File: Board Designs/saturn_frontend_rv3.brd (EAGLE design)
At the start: 40 parts

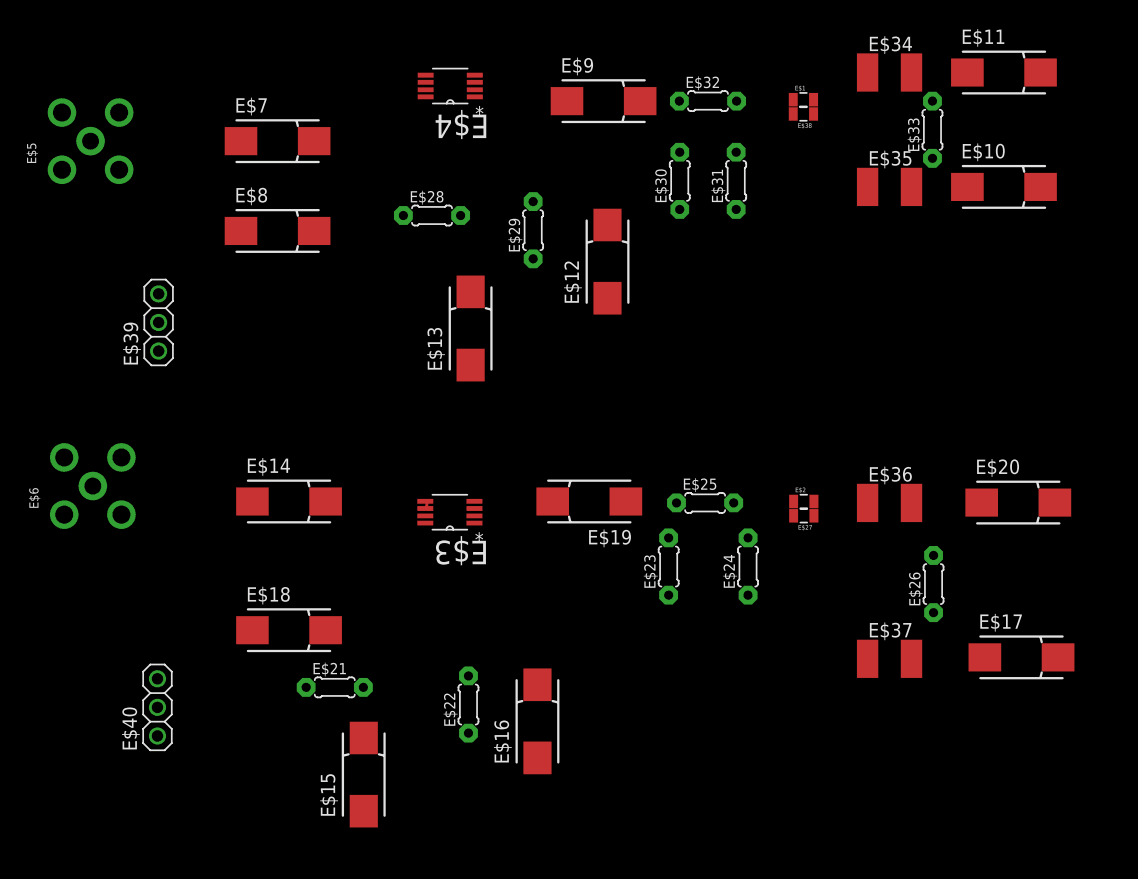
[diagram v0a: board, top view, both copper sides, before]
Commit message: Moved board designs to a seperate directory to keep SPICE/ clean
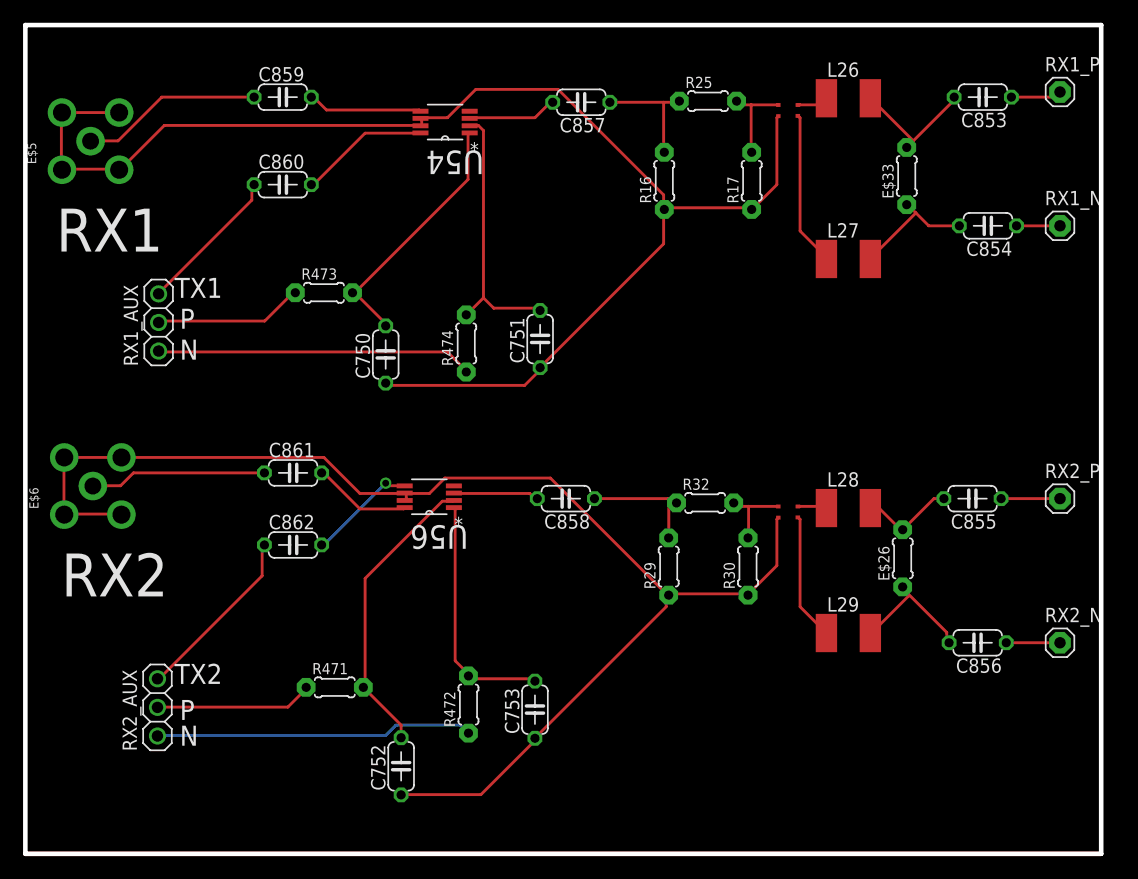
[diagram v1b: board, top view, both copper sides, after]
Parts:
- removed E$10, E$11, E$12, E$13, E$14, E$15, E$16, E$17, E$18, E$19, E$20, E$7, E$8, E$9: 100 pF, adafruit:085CS_1AR
- removed E$27, E$38: (no value), 0805:0805
- removed E$28, E$29: 100 Ohm, adafruit:0204/5
- removed E$3, E$4: (no value), SOP65P490X110-8N:SOP65P490X110-8N
- removed E$30, E$31: 221 Ohm, adafruit:0204/5
- removed E$34, E$35, E$36, E$37: 1.0 nH, eagle-ltspice:L1812
- added C750, C751, C752, C753, C853, C854, C855, C856, C857, C858, C859, C860, C861: 100 pF, adafruit:C050-024X044
- added C862: (no value), adafruit:C050-024X044
- added L26, L27, L28, L29: 1.0 nH, eagle-ltspice:L1812
- added R16, R17: 221 Ohm, adafruit:0204/5
- added R473, R474: 100 Ohm, adafruit:0204/5
- added RX1_N, RX1_P, RX2_N, RX2_P: (no value), adafruit:1X01
- added U54, U56: (no value), SOP65P490X110-8N:SOP65P490X110-8N
- E$1, E$2: device 0805:0805 -> cody_custom_library:BALUN_LOGICALS
- moved E$33 4.71 mm to (87.9, 72.1)
- moved E$26 3.57 mm to (87.5, 38.1)
- moved E$2 2.86 mm to (76.4, 41.6)
- moved E$1 2.85 mm to (76.4, 77.3)
- renumbered E$21 to R471, E$22 to R472, E$23 to R29, E$24 to R30, E$25 to R32, E$32 to R25, E$39 to RX1_AUX, E$40 to RX2_AUX
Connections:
- removed net S$17: E$2.1, R30.2, R32.2
- removed net S$21: E$12.-, E$13.-, E$30.1, E$31.1, E$38.2, E$4.6, E$4.7, E$5.GND3
- removed net S$22: E$28.2, E$4.1
- removed net S$26: E$30.2, E$9.+, R25.1
- new net S$1: E$2.1, R30.2, R32.2
- new net S$10: C857.1, R16.2, R25.1
- new net S$19: C854.2, E$33.1, L27.2
- new net S$35: C861.1, E$6.ANTENNA
- new net S$46: C752.1, C753.1, E$2.2, E$6.GND1, E$6.GND2, E$6.GND3, E$6.GND4, R29.1, R30.1, U56.6, U56.7
- new net S$47: C856.1, RX2_N.1
- new net S$49: R472.1, RX2_AUX.1
- net S$12: now also E$1.1, R17.2, R25.2; no longer E$11.-, E$33.2, E$34.2
- net S$14: now also E$1.4, L26.1; no longer E$14.+, E$15.-, E$16.-, E$27.2, E$3.5, E$3.6, E$3.7, E$6.GND3, R29.1, R30.1
- net S$16: now also E$1.3, L27.1; no longer E$4.5, E$7.+
- net S$18: now also C853.2, E$33.2, L26.2; no longer E$4.8, E$8.+
- net S$2: now also E$2.4, L28.1; no longer E$13.+
- net S$23: now also C853.1, RX1_P.1; no longer E$29.2, E$4.2
- net S$24: now also C854.1, RX1_N.1; no longer E$2.2, E$36.1
- net S$25: now also R473.1, RX1_AUX.2; no longer E$29.1, RX1_AUX.1
- net S$27: now also C750.2, R473.2, U54.1; no longer E$1.1, E$31.2, R25.2
- net S$28: now also C751.2, R474.2, U54.2; no longer E$1.2, E$34.1
- net S$29: now also R474.1, RX1_AUX.1; no longer E$35.1, E$38.1
- net S$3: now also C858.1, R29.2, R32.1; no longer E$12.+
- net S$32: now also R471.1, RX2_AUX.2; no longer E$18.-, RX2_AUX.3
- net S$33: now also C752.2, R471.2, U56.2; no longer R471.1, RX2_AUX.2
- net S$34: now also C753.2, R472.2, U56.1; no longer R472.1, RX2_AUX.1
- net S$36: now also C862.1, RX2_AUX.3; no longer E$14.-, E$6.ANTENNA
- net S$37: now also C860.1, RX1_AUX.3; no longer E$4.3, E$9.-
- net S$38: now also C859.1, E$5.ANTENNA; no longer E$18.+, E$3.8
- net S$39: now also C859.2, U54.5; no longer E$19.+, E$3.3
- net S$40: now also C860.2, U54.8; no longer E$15.+, E$3.1, R471.2
- net S$41: now also C862.2, U56.5; no longer E$16.+, E$3.2, R472.2
- net S$42: now also C861.2, U56.8; no longer E$19.-, R29.2, R32.1
- net S$43: now also C858.2, U56.3; no longer E$27.1, E$37.1
- net S$44: now also C857.2, U54.3; no longer E$20.-, E$26.2, E$36.2
- net S$45: now also C750.1, C751.1, E$1.2, E$5.GND1, E$5.GND2, E$5.GND3, E$5.GND4, R16.1, R17.1, U54.6, U54.7; no longer E$17.-, E$26.1, E$37.2
- net S$5: now also C855.2, E$26.2, L28.2; no longer E$5.ANTENNA, E$7.-
- net S$6: now also C855.1, RX2_P.1; no longer E$10.-, E$33.1, E$35.2
- net S$7: now also C856.2, E$26.1, L29.2; no longer E$8.-, RX1_AUX.3
- net S$8: now also E$2.3, L29.1; no longer E$28.1, RX1_AUX.2
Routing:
- net S$45: track 0.00 -> 122.8 mm
- net S$46: track 0.00 -> 117.7 mm
- net S$48: track 0.00 -> 95.6 mm
- net S$49: track 0.00 -> 28.3 mm
- net S$29: track 0.00 -> 28.2 mm
- net S$33: track 0.00 -> 26.4 mm
- net S$28: track 0.00 -> 24.0 mm
- net S$27: track 0.18 -> 22.8 mm
- net S$34: track 0.00 -> 21.7 mm
- net S$38: track 0.00 -> 16.1 mm
- net S$36: track 0.00 -> 16.0 mm
- net S$35: track 0.00 -> 15.7 mm
- net S$16: track 0.00 -> 13.8 mm
- net S$32: track 0.36 -> 14.0 mm
- net S$25: track 0.00 -> 13.3 mm
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- added copper zone on layer 1, net GND
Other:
- board outline added: 95.6 x 73.6 mm
- board text added: "N"
- board text added: "P"
- board text added: "RX1"
- board text added: "RX2"
- board text added: "Saturn Front End MK4"
- board text added: "TX1"
- board text added: "TX2"
